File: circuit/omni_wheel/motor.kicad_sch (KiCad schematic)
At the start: 12 parts, among them J3 Conn_01x06_Male, J4 Conn_01x06_Male, J5 Conn_01x06_Male, U5 DRV8837, U6 DRV8837, U7 DRV8837

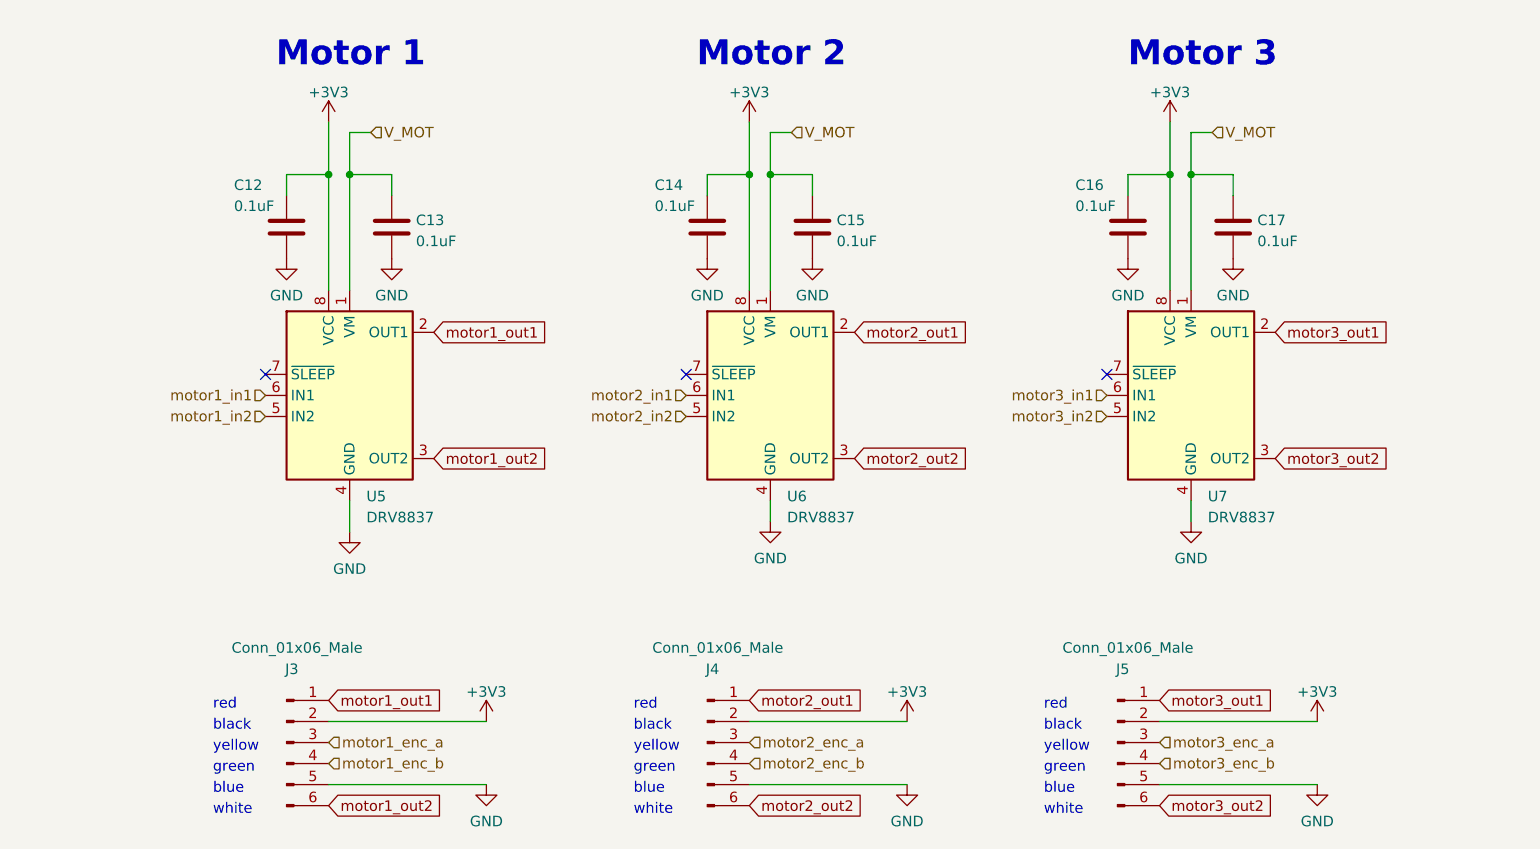
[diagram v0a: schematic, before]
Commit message: connect nsleep to high and remove unnecessary switch.
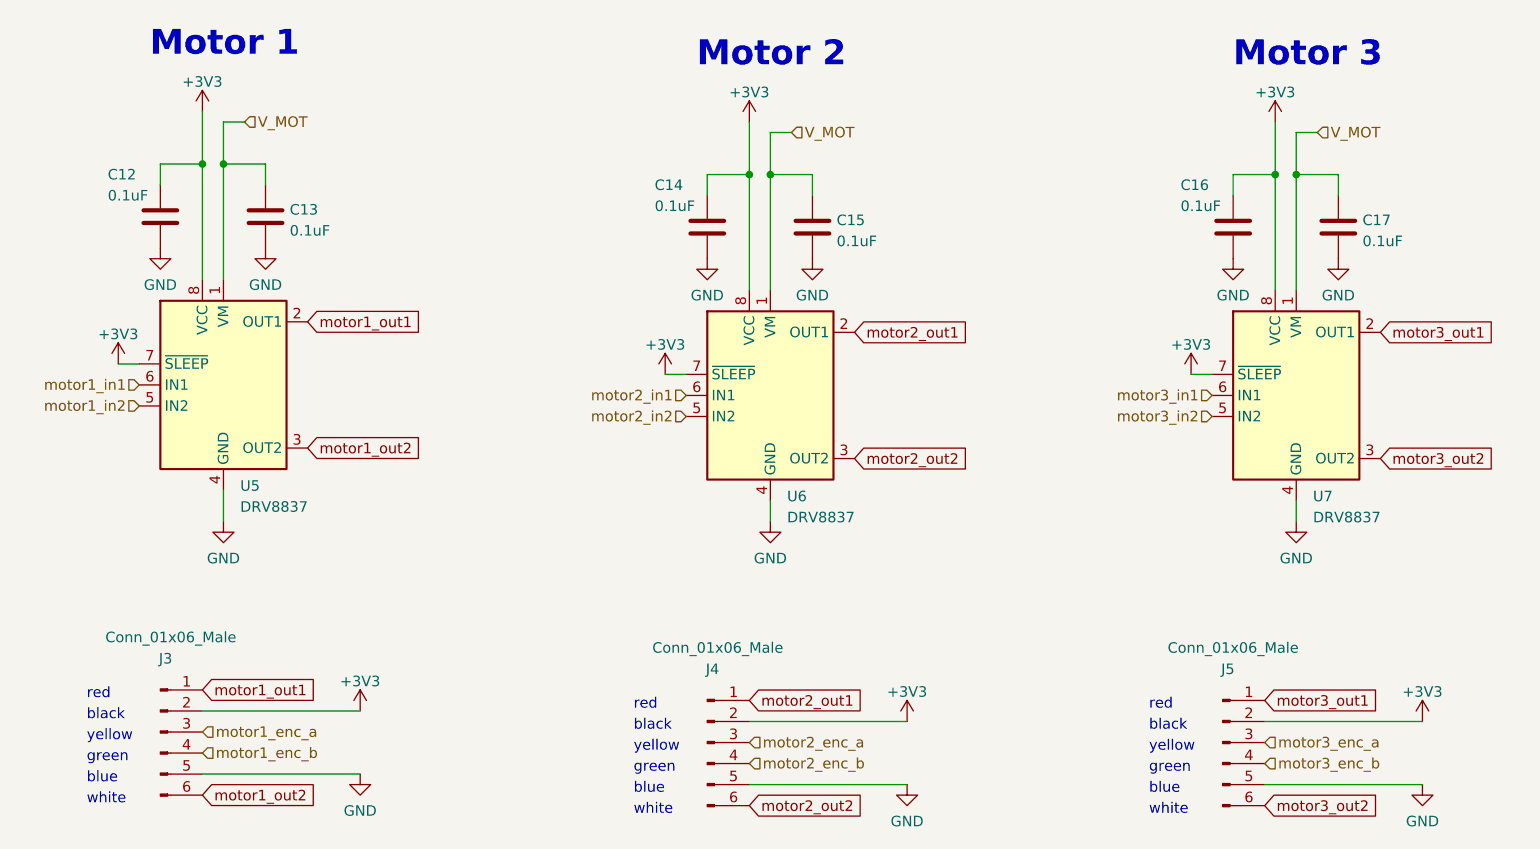
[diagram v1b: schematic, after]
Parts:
- J3, J4, J5: Vendor (none) -> https://www.digikey.jp/ja/products/detail/w%C3%BCrth-elektr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
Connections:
- net +3V3: now also U5.7 (~{SLEEP}), U6.7 (~{SLEEP}), U7.7 (~{SLEEP})
- no-connect marks 3 -> 0
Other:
- moved on the sheet: C12, C13, C16, C17, J3, J5, U5, U7
